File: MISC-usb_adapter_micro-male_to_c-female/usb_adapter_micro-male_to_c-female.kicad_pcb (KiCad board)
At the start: 2 copper layers, 14 x 11.5 mm, 6 parts, among them J2 USB2.0-C_SMT, J3 USB_B_Micro

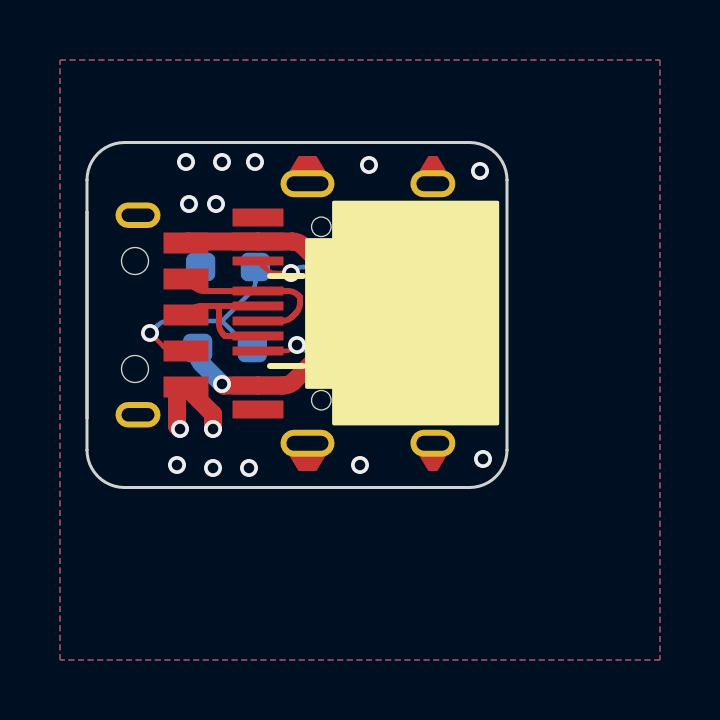
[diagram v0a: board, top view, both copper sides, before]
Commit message: usb_adapter_micro-male_to_c-female/1.0.0
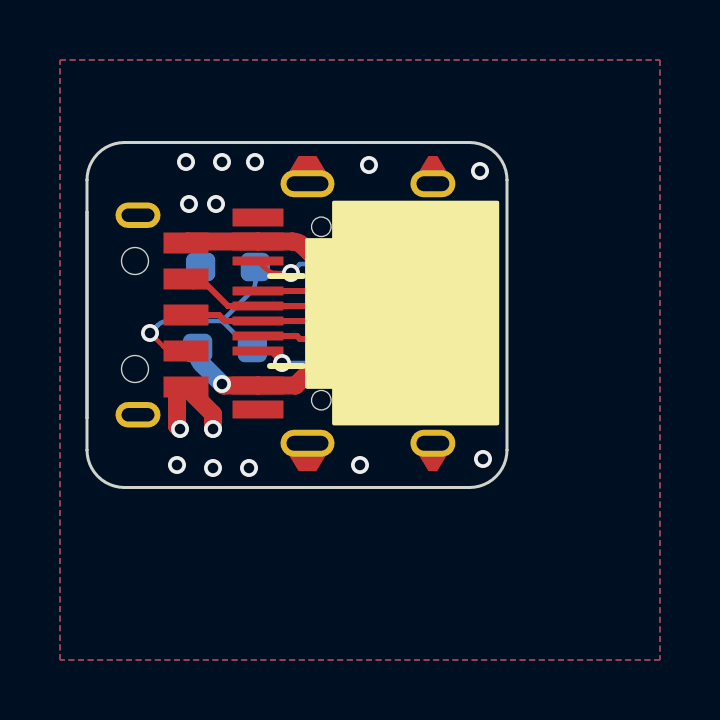
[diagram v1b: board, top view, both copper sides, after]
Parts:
- moved R2 1.79 mm to (73.8, 42.8)
- moved R1 1.60 mm to (73.8, 39.4)
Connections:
- J3 pad 2: Net-(J2-D+) -> Net-(J2-D-)
- J3 pad 3: Net-(J2-D-) -> Net-(J2-D+)
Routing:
- net Net-(J2-D-): track 4.70 -> 10.1 mm, vias 0 -> 2
- net Net-(J2-VBUS): track 13.1 -> 16.0 mm
- net Net-(J2-D+): track 5.92 -> 8.12 mm, vias 0 -> 2
- net Net-(J2-CC1): track 2.22 -> 4.32 mm
- net Net-(J2-CC2): track 2.39 -> 4.24 mm
